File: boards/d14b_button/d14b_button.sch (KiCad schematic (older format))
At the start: 56 parts, among them CON1 USB-MICRO-B, P1 CONN_02X05, P2 CONN_01X03, P3 PIEZO_BUZZ, P4 EEPROM_SPI, Q1 MOSFET_N, SW1 SW_PUSH, SW2 SW_PUSH, SW3 SW_PUSH, SW4 SW_PUSH, U1 nRF24L01+-Module, U2 STM32F030C8T6, U3 TPS61221, X1 8M, X2 32.768k

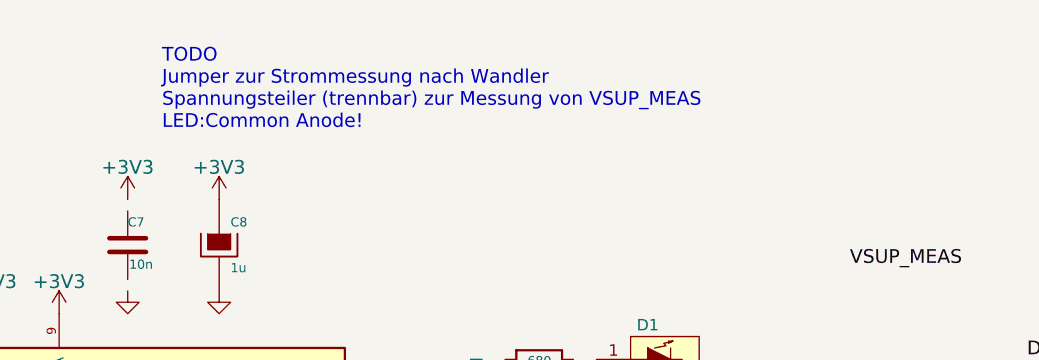
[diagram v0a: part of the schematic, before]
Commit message: TODO zu Schaltplan ergänzt
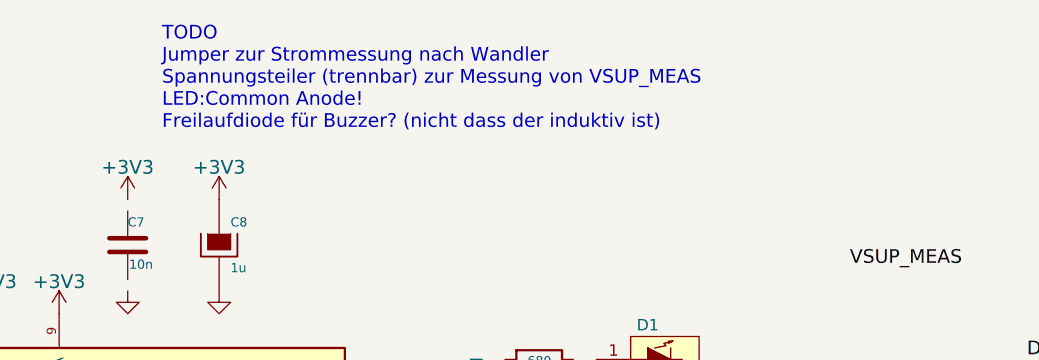
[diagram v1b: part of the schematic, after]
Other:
- note added: "TODO\nJumper zur Strommessung nach Wandler\nSpannungsteiler (trennbar) zur Messung von VSUP_MEAS\nLED:Common Anode!\nFreilaufdiode für Buzzer? (nicht dass der induktiv ist)"
- note removed: "TODO\nJumper zur Strommessung nach Wandler\nSpannungsteiler (trennbar) zur Messung von VSUP_MEAS\nLED:Common Anode!"
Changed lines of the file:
@@
 	9050 3350 9350 3350
 Text Notes 3950 850  0    60   ~ 0
-TODO\nJumper zur Strommessung nach Wandler\nSpannungsteiler (trennbar) zur Messung von VSUP_MEAS\nLED:Common Anode!
+TODO\nJumper zur Strommessung nach Wandler\nSpannungsteiler (trennbar) zur Messung von VSUP_MEAS\nLED:Common Anode!\nFreilaufdiode für Buzzer? (nicht dass der induktiv ist)
 Wire Wire Line
 	8900 1000 9650 1000

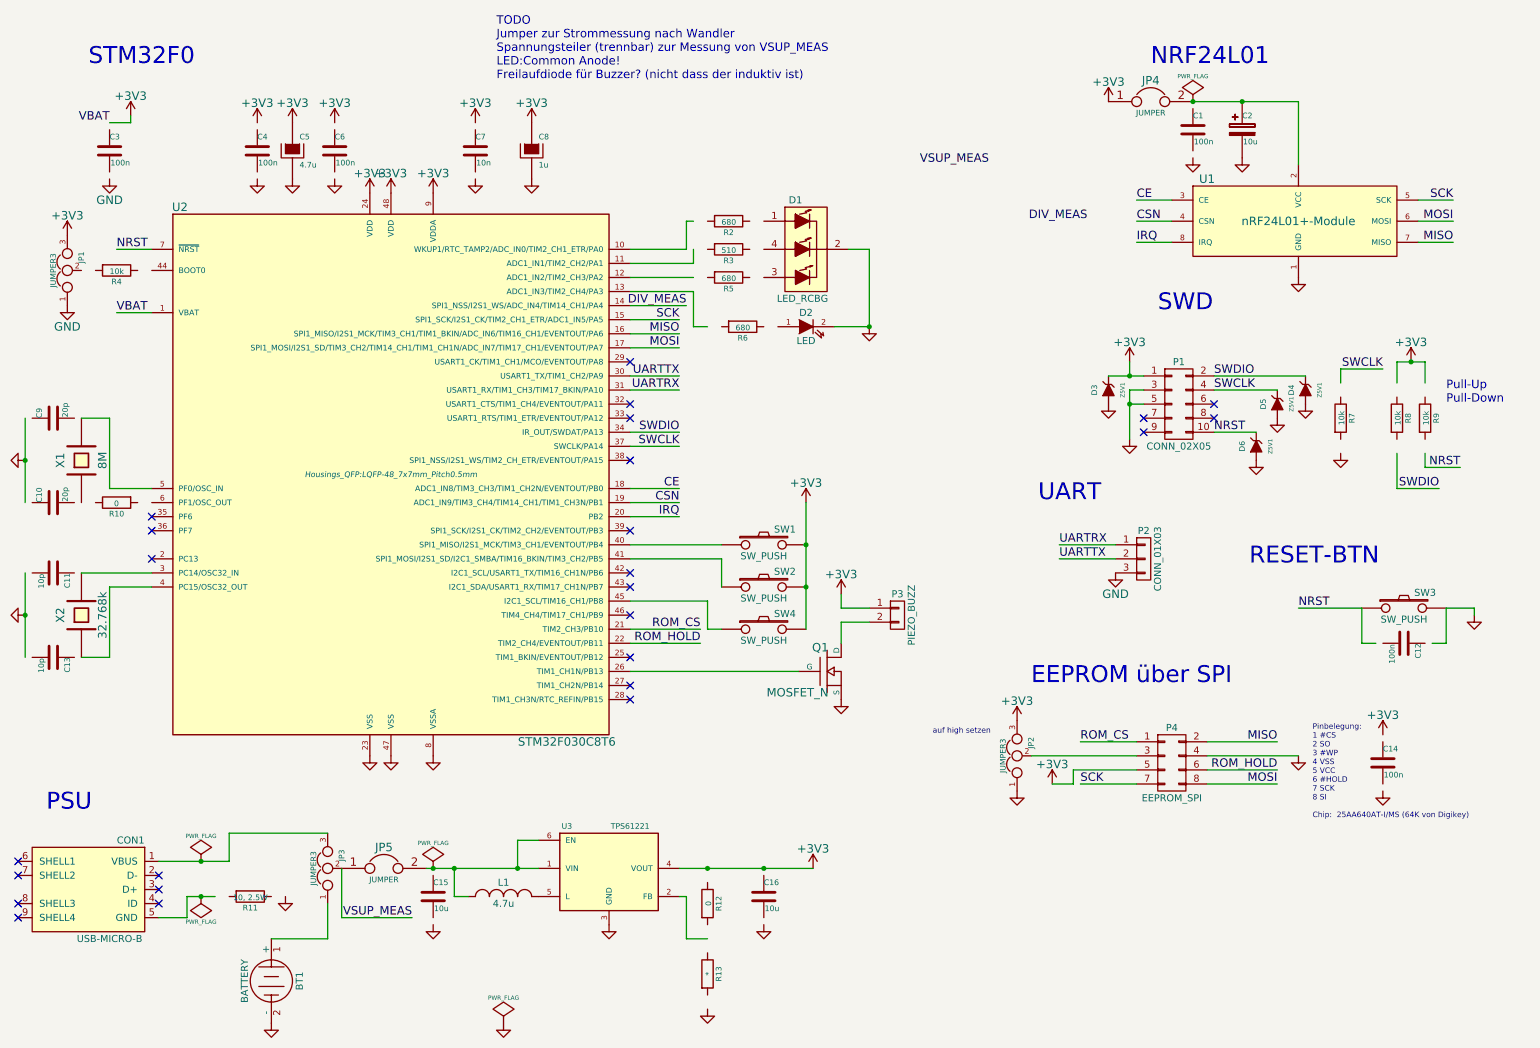
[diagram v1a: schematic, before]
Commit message: TODOs im Schaltplan abgebaut, Spannungsmessung, Strommessung...
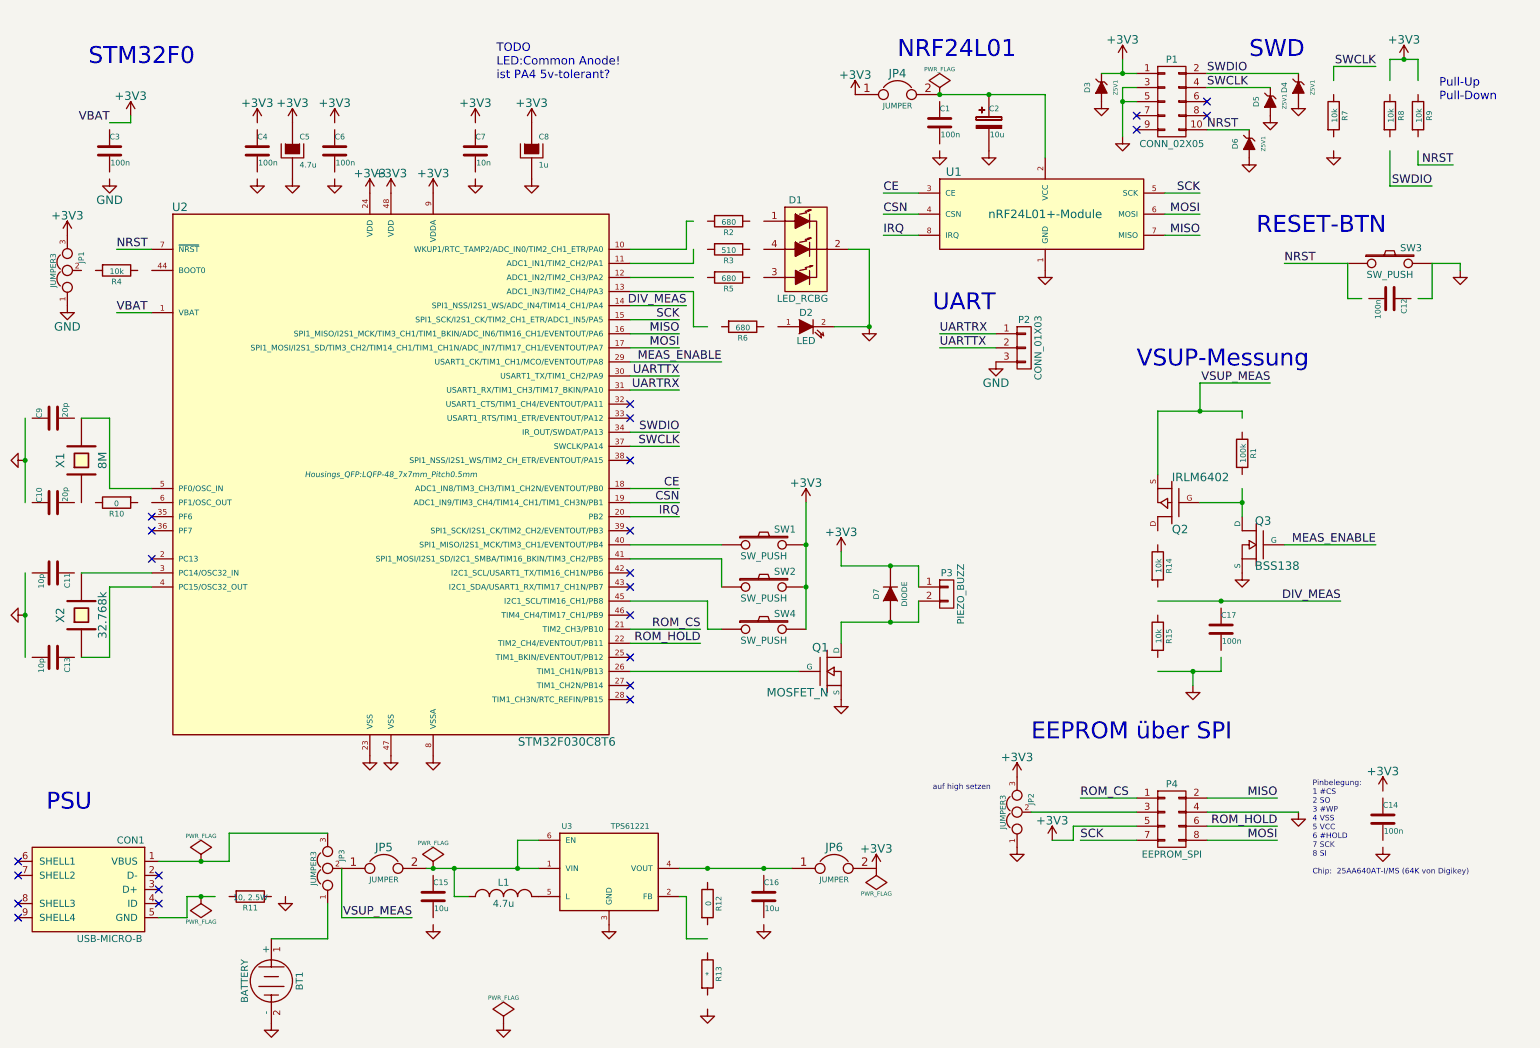
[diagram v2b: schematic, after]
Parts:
- added C17: 100n, symbol C
- added D7: DIODE, symbol DIODE
- added JP6: JUMPER, symbol JUMPER
- added Q2: IRLM6402, symbol MOSFET_P
- added Q3: BSS138, symbol MOSFET_N
- added R1: 100k, symbol R
- added R14, R15: 10k, symbol R
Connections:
- net labels added: MEAS_ENABLE
- wire segments 113 -> 128
- no-connect marks 25 -> 24
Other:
- note added: "TODO\nLED:Common Anode!\nist PA4 5v-tolerant?"
- note added: "VSUP-Messung"
- note removed: "TODO\nJumper zur Strommessung nach Wandler\nSpannungsteiler (trennbar) zur Messung von VSUP_MEAS\nLED:Common Anode!\nFreilaufdiode für Buzzer? (nicht dass der induktiv ist)"
- moved on the sheet: C1, C12, C14, C2, D3, D4, D5, D6, JP2, JP4, P1, P2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

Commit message: alle TODOs aus Schaltplan erledigt
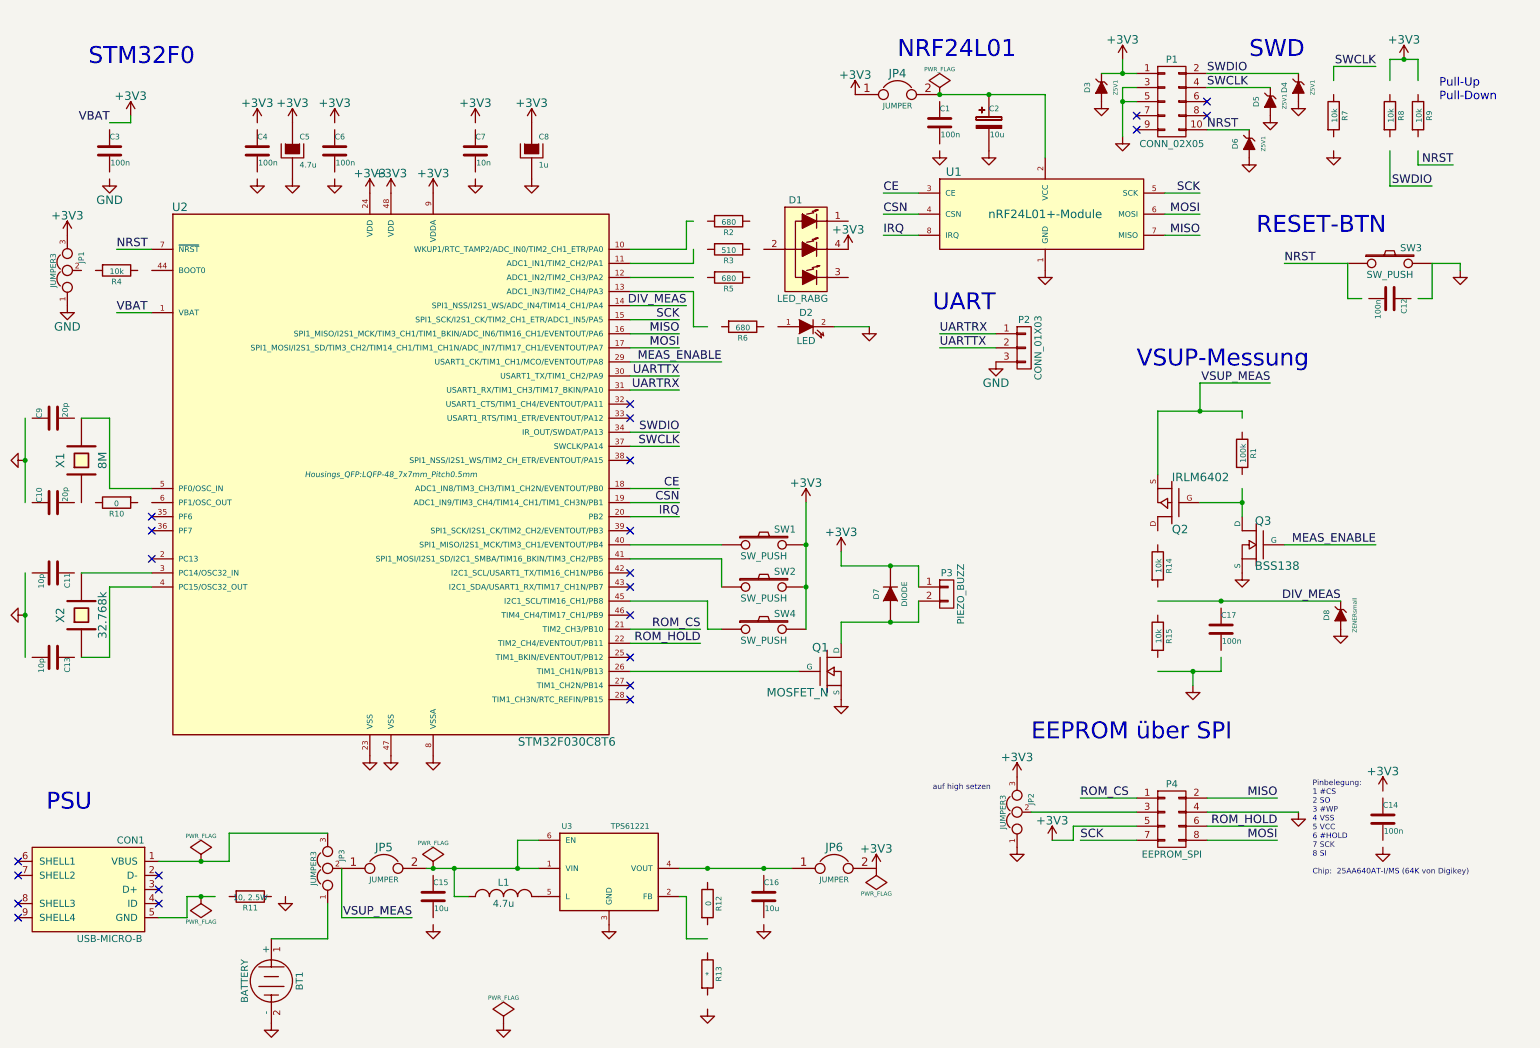
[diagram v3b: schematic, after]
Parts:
- removed D1: LED_RCBG, Pin_Headers:Pin_Header_Straight_2x02, symbol LED_RCBG
- added D1: LED_RABG, symbol LED_RABG
- added D8: ZENERsmall, symbol ZENERsmall
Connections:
- wire segments 128 -> 126
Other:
- note removed: "TODO\nLED:Common Anode!\nist PA4 5v-tolerant?"
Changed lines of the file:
@@
 LIBS:tps61221
 LIBS: STM32F030C8T6
+LIBS:led_rabg
 LIBS:d14b_button-cache
 EELAYER 25 0
@@
 Sheet 1 1
 Title "Cowbus Demoboard (Schaltermodul)"
-Date "Fr 09 Jan 2015"
-Rev "2"
+Date "Mo 19 Jan 2015"
+Rev "3"
 Comp "https://michz.github.io/diy14bus/"
 Comment1 ""
@@
 	1    5600 1850
 	0    1    1    0
-$EndComp
-$Comp
-L LED_RCBG D1
-U 1 1 54AFC019
-P 6150 2050
-F 0 "D1" H 6075 2400 50  0000 C CNN
-F 1 "LED_RCBG" H 6125 1700 50  0000 C CNN
-F 2 "Pin_Headers:Pin_Header_Straight_2x02" H 6150 2000 50  0001 C CNN
-F 3 "" H 6150 2000 50  0000 C CNN
-	1    6150 2050
-	1    0    0    -1
 $EndComp
 $Comp
@@
 $EndComp
 Wire Wire Line
-	6450 2050 6600 2050
-Wire Wire Line
-	6600 2050 6600 2600
-Wire Wire Line
 	6600 2600 6350 2600
-Connection ~ 6600 2600
 Wire Wire Line
 	5350 2600 5450 2600
@@
 Wire Wire Line
 	9000 1200 9300 1200
-Text Notes 3950 850  0    60   ~ 0
-TODO\nLED:Common Anode!\nist PA4 5v-tolerant?
 Wire Wire Line
 	7100 950  7850 950
@@
 	-1   0    0    1
 $EndComp
+$Comp
+L ZENERsmall D8
+U 1 1 54BF6E88
+P 9950 4650
+F 0 "D8" H 9950 4750 40  0000 C CNN
+F 1 "ZENERsmall" H 9950 4550 30  0000 C CNN
+F 2 "" H 9950 4650 60  0000 C CNN
+F 3 "" H 9950 4650 60  0000 C CNN
+	1    9950 4650
+	0    -1   -1   0
+$EndComp
+$Comp
+L GND #PWR063
+U 1 1 54BF6FB3
+P 9950 4750
+F 0 "#PWR063" H 9950 4750 30  0001 C CNN
+F 1 "GND" H 9950 4680 30  0001 C CNN
+F 2 "" H 9950 4750 60  0000 C CNN
+F 3 "" H 9950 4750 60  0000 C CNN
+	1    9950 4750
+	1    0    0    -1
+$EndComp
+$Comp
+L LED_RABG D1
+U 1 1 54BFA583
+P 6150 2050
+F 0 "D1" H 6075 2400 50  0000 C CNN
+F 1 "LED_RABG" H 6125 1700 50  0000 C CNN
+F 2 "" H 6100 2200 50  0000 C CNN
+F 3 "" H 6100 2200 50  0000 C CNN
+	1    6150 2050
+	1    0    0    -1
+$EndComp
+$Comp
+L +3V3 #PWR064
+U 1 1 54BFA9A1
+P 6450 2050
+F 0 "#PWR064" H 6450 1900 60  0001 C CNN
+F 1 "+3V3" H 6450 2190 60  0000 C CNN
+F 2 "" H 6450 2050 60  0000 C CNN
+F 3 "" H 6450 2050 60  0000 C CNN
+	1    6450 2050
+	1    0    0    -1
+$EndComp
 $EndSCHEMATC

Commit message: added all footprints but the crystals
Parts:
- BT1: footprint (none) -> batteryconn:KZH20SMD-2
- C17: footprint (none) -> Capacitors_SMD:C_0603
- C8: footprint Capacitors_SMD:c_elec_4x5.8 -> Capacitors_SMD:C_0603
- D1: footprint (none) -> d14lib:PLCC-4
- D7, D8: footprint (none) -> Diodes_SMD:Diode-MiniMELF_Standard
- JP1, JP2, JP3: footprint Connect:GS3 -> Connect:PINHEAD1-3
- JP4, JP5, JP6: footprint (none) -> Connect:PINHEAD1-2
- L1: footprint (none) -> d14lib:NRS8030
- P1: footprint Connect:VASCH10x2 -> d14lib:CORTEX_header_SMD
- Q1: footprint SMD_Packages:DPAK-2-1EP_GDS -> SMD_Packages:SOT-23-GDS
- Q2, Q3: footprint (none) -> SMD_Packages:SOT-23-GDS
- R1, R14, R15: footprint (none) -> Resistors_SMD:R_0603
- R11: footprint Resistors_ThroughHole:Resistor_Horizontal_RM15mm -> Resistors_ThroughHole:Resistor_Horizontal_RM20mm
- R8: footprint Resistors_ThroughHole:Resistor_Horizontal_RM15mm -> Resistors_SMD:R_0603
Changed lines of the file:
@@
 F 0 "BT1" H 2350 7450 50  0000 C CNN
 F 1 "BATTERY" H 2350 7060 50  0000 C CNN
-F 2 "" H 2350 7250 60  0001 C CNN
+F 2 "batteryconn:KZH20SMD-2" H 2350 7250 60  0001 C CNN
 F 3 "" H 2350 7250 60  0000 C CNN
 	1    2350 7250
@@
 F 0 "L1" H 4000 6750 50  0000 C CNN
 F 1 "4.7u" H 4000 6600 50  0000 C CNN
-F 2 "" H 4000 6650 60  0001 C CNN
+F 2 "d14lib:NRS8030" H 4000 6650 60  0001 C CNN
 F 3 "" H 4000 6650 60  0000 C CNN
 	1    4000 6650
@@
 F 0 "JP1" H 950 2100 40  0000 L CNN
 F 1 "JUMPER3" H 900 2300 40  0000 C CNN
-F 2 "Connect:GS3" H 900 2200 60  0001 C CNN
+F 2 "Connect:PINHEAD1-3" H 900 2200 60  0001 C CNN
 F 3 "" H 900 2200 60  0000 C CNN
 	1    900  2200
@@
 F 0 "C8" H 4250 1450 40  0000 L CNN
 F 1 "1u" H 4250 1250 40  0000 L CNN
-F 2 "Capacitors_SMD:c_elec_4x5.8" H 4300 1200 30  0001 C CNN
+F 2 "Capacitors_SMD:C_0603" H 4300 1200 30  0001 C CNN
 F 3 "" H 4200 1350 300 0000 C CNN
 	1    4200 1350
@@
 F 0 "JP3" H 2800 6350 40  0000 L CNN
 F 1 "JUMPER3" H 2750 6550 40  0000 C CNN
-F 2 "Connect:GS3" H 2750 6450 60  0001 C CNN
+F 2 "Connect:PINHEAD1-3" H 2750 6450 60  0001 C CNN
 F 3 "" H 2750 6450 60  0000 C CNN
 	1    2750 6450
@@
 F 0 "Q1" H 6310 5220 60  0000 R CNN
 F 1 "MOSFET_N" H 6310 4900 60  0000 R CNN
-F 2 "SMD_Packages:DPAK-2-1EP_GDS" H 6300 5050 60  0001 C CNN
+F 2 "SMD_Packages:SOT-23-GDS" H 6300 5050 60  0001 C CNN
 F 3 "" H 6300 5050 60  0000 C CNN
 	1    6300 5050
@@
 F 0 "R11" V 2280 6650 40  0000 C CNN
 F 1 "10, 2.5W" V 2207 6651 40  0000 C CNN
-F 2 "Resistors_ThroughHole:Resistor_Horizontal_RM15mm" V 2130 6650 30  0001 C CNN
+F 2 "Resistors_ThroughHole:Resistor_Horizontal_RM20mm" V 2130 6650 30  0001 C CNN
 F 3 "" H 2200 6650 30  0000 C CNN
 	1    2200 6650
@@
 F 0 "JP2" H 7700 5950 40  0000 L CNN
 F 1 "JUMPER3" H 7650 6150 40  0000 C CNN
-F 2 "Connect:GS3" H 7650 6050 60  0001 C CNN
+F 2 "Connect:PINHEAD1-3" H 7650 6050 60  0001 C CNN
 F 3 "" H 7650 6050 60  0000 C CNN
 	1    7650 6050
@@
 F 0 "R8" V 10380 1100 40  0000 C CNN
 F 1 "10k" V 10307 1101 40  0000 C CNN
-F 2 "Resistors_ThroughHole:Resistor_Horizontal_RM15mm" V 10230 1100 30  0001 C CNN
+F 2 "Resistors_SMD:R_0603" V 10230 1100 30  0001 C CNN
 F 3 "" H 10300 1100 30  0000 C CNN
 	1    10300 1100
@@
 F 0 "P1" H 8750 1300 50  0000 C CNN
 F 1 "CONN_02X05" H 8750 700 50  0000 C CNN
-F 2 "Connect:VASCH10x2" H 8750 -200 60  0001 C CNN
+F 2 "d14lib:CORTEX_header_SMD" H 8750 -200 60  0001 C CNN
 F 3 "" H 8750 -200 60  0000 C CNN
 	1    8750 1000
@@
 F 0 "JP4" H 6800 1100 60  0000 C CNN
 F 1 "JUMPER" H 6800 870 40  0000 C CNN
-F 2 "" H 6800 950 60  0000 C CNN
+F 2 "Connect:PINHEAD1-2" H 6800 950 60  0001 C CNN
 F 3 "" H 6800 950 60  0000 C CNN
 	1    6800 950
@@
 F 0 "JP5" H 3150 6600 60  0000 C CNN
 F 1 "JUMPER" H 3150 6370 40  0000 C CNN
-F 2 "" H 3150 6450 60  0000 C CNN
+F 2 "Connect:PINHEAD1-2" H 3150 6450 60  0001 C CNN
 F 3 "" H 3150 6450 60  0000 C CNN
 	1    3150 6450
@@
 F 0 "D7" H 6750 4600 40  0000 C CNN
 F 1 "DIODE" H 6750 4400 40  0000 C CNN
-F 2 "" H 6750 4500 60  0000 C CNN
+F 2 "Diodes_SMD:Diode-MiniMELF_Standard" H 6750 4500 60  0001 C CNN
 F 3 "" H 6750 4500 60  0000 C CNN
 	1    6750 4500
@@
 F 0 "Q3" H 9360 4320 60  0000 R CNN
 F 1 "BSS138" H 9360 4000 60  0000 R CNN
-F 2 "" H 9350 4150 60  0000 C CNN
+F 2 "SMD_Packages:SOT-23-GDS" H 9350 4150 60  0001 C CNN
 F 3 "" H 9350 4150 60  0000 C CNN
 	1    9350 4150
@@
 F 0 "Q2" H 8750 4040 60  0000 R CNN
 F 1 "IRLM6402" H 8750 3670 60  0000 R CNN
-F 2 "" H 8750 3850 60  0000 C CNN
+F 2 "SMD_Packages:SOT-23-GDS" H 8750 3850 60  0001 C CNN
 F 3 "" H 8750 3850 60  0000 C CNN
 	1    8750 3850
@@
 F 0 "R1" V 9330 3500 40  0000 C CNN
 F 1 "100k" V 9257 3501 40  0000 C CNN
-F 2 "" V 9180 3500 30  0000 C CNN
+F 2 "Resistors_SMD:R_0603" V 9180 3500 30  0001 C CNN
 F 3 "" H 9250 3500 30  0000 C CNN
 	1    9250 3500
@@
 F 0 "R14" V 8730 4300 40  0000 C CNN
 F 1 "10k" V 8657 4301 40  0000 C CNN
-F 2 "" V 8580 4300 30  0000 C CNN
+F 2 "Resistors_SMD:R_0603" V 8580 4300 30  0001 C CNN
 F 3 "" H 8650 4300 30  0000 C CNN
 	1    8650 4300
@@
 F 0 "R15" V 8730 4800 40  0000 C CNN
 F 1 "10k" V 8657 4801 40  0000 C CNN
-F 2 "" V 8580 4800 30  0000 C CNN
+F 2 "Resistors_SMD:R_0603" V 8580 4800 30  0001 C CNN
 F 3 "" H 8650 4800 30  0000 C CNN
 	1    8650 4800
@@
 F 0 "C17" H 9100 4850 40  0000 L CNN
 F 1 "100n" H 9106 4665 40  0000 L CNN
-F 2 "" H 9138 4600 30  0000 C CNN
+F 2 "Capacitors_SMD:C_0603" H 9138 4600 30  0001 C CNN
 F 3 "" H 9100 4750 60  0000 C CNN
 	1    9100 4750
@@
 F 0 "JP6" H 6350 6600 60  0000 C CNN
 F 1 "JUMPER" H 6350 6370 40  0000 C CNN
-F 2 "" H 6350 6450 60  0000 C CNN
+F 2 "Connect:PINHEAD1-2" H 6350 6450 60  0001 C CNN
 F 3 "" H 6350 6450 60  0000 C CNN
 	1    6350 6450
@@
 F 0 "D8" H 9950 4750 40  0000 C CNN
 F 1 "ZENERsmall" H 9950 4550 30  0000 C CNN
-F 2 "" H 9950 4650 60  0000 C CNN
+F 2 "Diodes_SMD:Diode-MiniMELF_Standard" H 9950 4650 60  0001 C CNN
 F 3 "" H 9950 4650 60  0000 C CNN
 	1    9950 4650
@@
 F 0 "D1" H 6075 2400 50  0000 C CNN
 F 1 "LED_RABG" H 6125 1700 50  0000 C CNN
-F 2 "" H 6100 2200 50  0000 C CNN
+F 2 "d14lib:PLCC-4" H 6100 2200 50  0001 C CNN
 F 3 "" H 6100 2200 50  0000 C CNN
 	1    6150 2050

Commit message: alle Footprints hinzugefügt und zugeordnet
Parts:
- X1: footprint (none) -> Crystals:Crystal_HC49-SD_SMD
- X2: footprint (none) -> d14lib:crystal_SMD_CPFB
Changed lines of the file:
@@
 F 0 "X1" H 1000 3700 60  0000 C CNN
 F 1 "8M" H 1000 3400 60  0000 C CNN
-F 2 "" H 1000 3550 60  0001 C CNN
+F 2 "Crystals:Crystal_HC49-SD_SMD" H 1000 3550 60  0001 C CNN
 F 3 "" H 1000 3550 60  0000 C CNN
 	1    1000 3550
@@
 F 0 "X2" H 1000 4800 60  0000 C CNN
 F 1 "32.768k" H 1000 4500 60  0000 C CNN
-F 2 "" H 1000 4650 60  0001 C CNN
+F 2 "d14lib:crystal_SMD_CPFB" H 1000 4650 60  0001 C CNN
 F 3 "" H 1000 4650 60  0000 C CNN
 	1    1000 4650

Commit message: Bauteile platziert
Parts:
- JP2: footprint Connect:PINHEAD1-3 -> Oddities:NetTie-II_SMD
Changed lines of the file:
@@
 F 0 "JP2" H 7700 5950 40  0000 L CNN
 F 1 "JUMPER3" H 7650 6150 40  0000 C CNN
-F 2 "Connect:PINHEAD1-3" H 7650 6050 60  0001 C CNN
+F 2 "Oddities:NetTie-II_SMD" H 7650 6050 60  0001 C CNN
 F 3 "" H 7650 6050 60  0000 C CNN
 	1    7650 6050
